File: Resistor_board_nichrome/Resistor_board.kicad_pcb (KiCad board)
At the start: 2 copper layers, 39 x 12.8 mm, 6 parts, among them J1 Conn_01x06_Pin, SW1 SW_SPDT_312

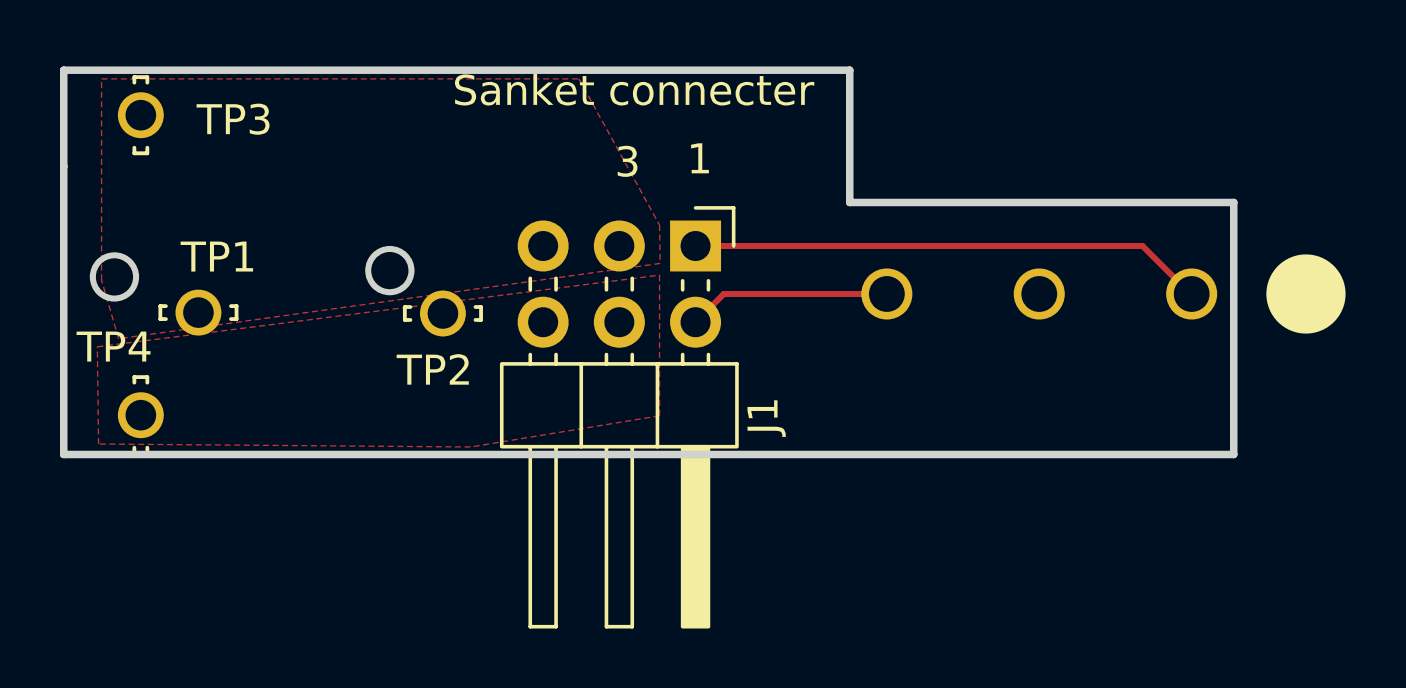
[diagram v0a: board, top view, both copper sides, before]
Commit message: Added step file for ADS_V8
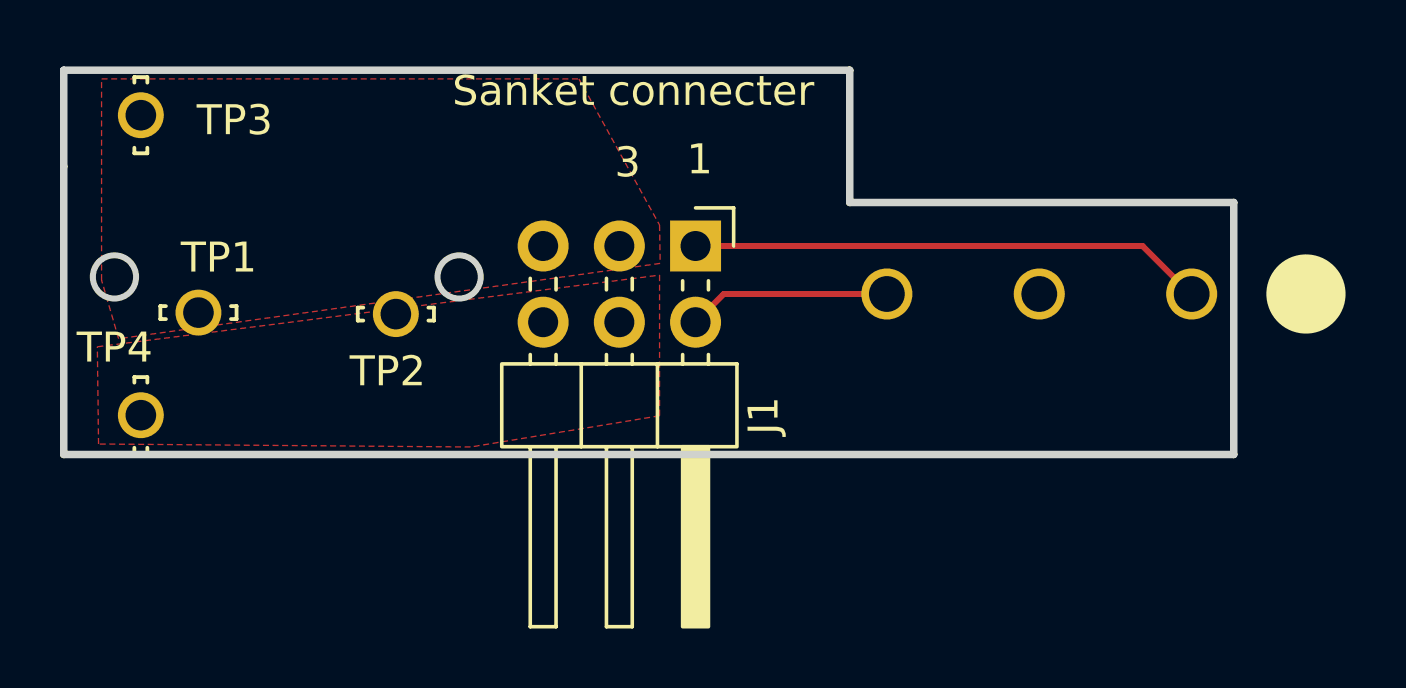
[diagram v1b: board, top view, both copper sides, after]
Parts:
- moved TP2 1.57 mm to (121.0, 59.6)
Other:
- outline, holes or cut-outs redrawn
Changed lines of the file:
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@@
 	(footprint "5021:TP_5021"
 		(layer "F.Cu")
-		(at 122.58 59.55)
+		(at 121.01 59.57)
 		(property "Reference" "TP2"
 			(at -0.27 1.91 0)
@@
 	)
 	(gr_circle
-		(center 120.81 58.12)
-		(end 121.41 58.52)
+		(center 123.12 58.33111)
+		(end 123.84111 58.33111)
 		(stroke
 			(width 0.2)
